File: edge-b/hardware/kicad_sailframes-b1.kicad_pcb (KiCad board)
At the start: 2 copper layers, 79.3 x 73.9 mm, 72 parts, among them J2 JST_PH_BAT, J3 U.FL, J5 MICROSD, J8 BNO085_SOCKET, J9 HOSYOND_3.5_TFT, U1 LC29HEAMD, U2 TP4056, U3 MT3608, U4 ESP32_DEVKIT_V1

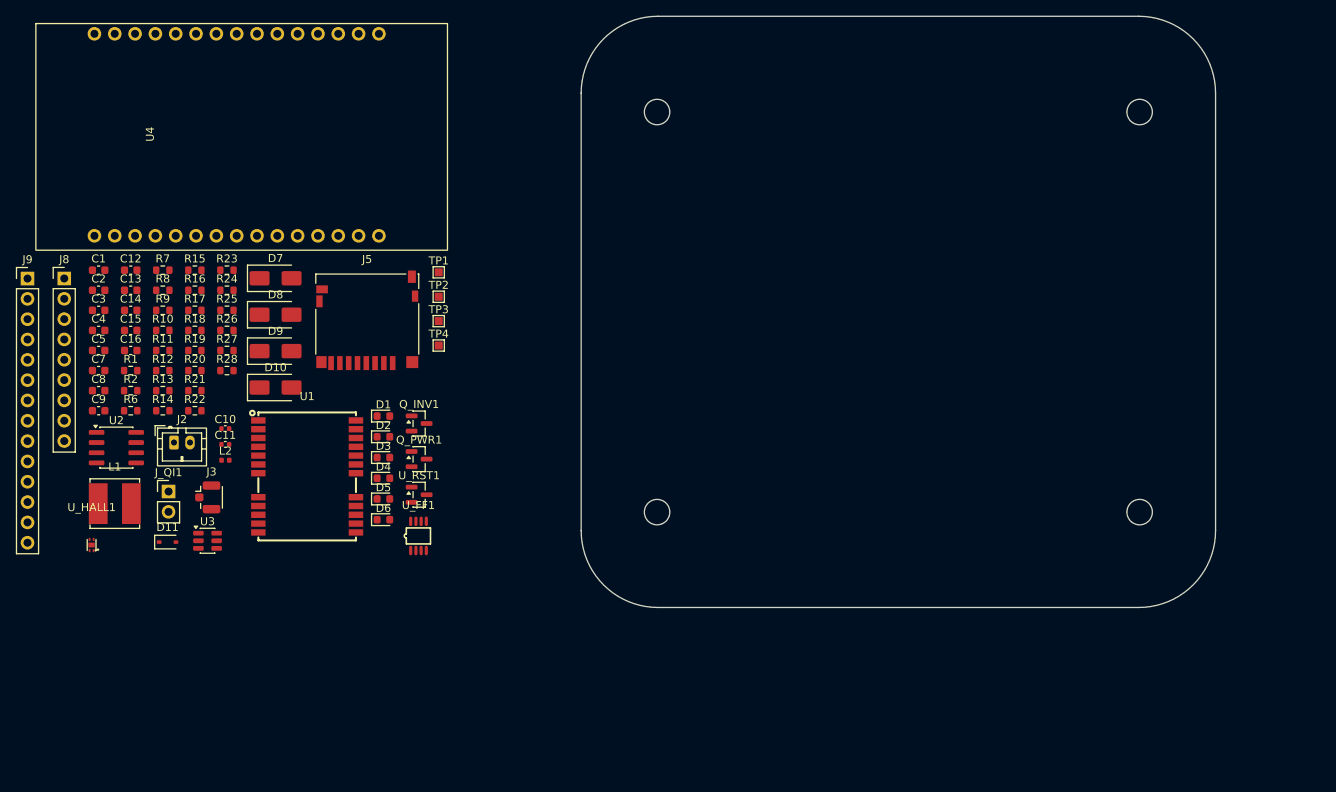
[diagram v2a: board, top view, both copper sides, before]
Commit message: B1 PCB: footprints placed, DRC clean (0 errors)
Update PCB from Schematic synced all 50 components + 6 expansion
connectors (J10-J15) onto the v0.12 outline. Initial placement done
manually in KiCad:

- ESP32 (U4) on B.Cu — wait, on F.Cu (B.Cu reserved for battery contact)
- All components on F.Cu (no components on B.Cu, battery sits underneath)
- L1 boost inductor positioned away from U_HALL1 (magnetic isolation)
- GNSS block (U1, L2, C10, C11, J3) at top-left, RF-clean area
- Power chain (TP4056, MT3608, hall latch) clustered bottom-right
- TFT connector (J9) along bottom edge for cover-side mounting
- microSD (J5) accessible from edge

Board Setup adjustments:
- Default netclass clearance: 0.3 → 0.2 mm (small-pitch IC packages
  like U_HALL1 X2SON-4 and U_FF1 SM8 don't meet 0.3 mm)
- Minimum hole diameter: 0.3 → 0.2 mm (TP4056 SOIC-8-1EP thermal vias)

DRC: 0 errors, 29 cosmetic warnings (silk_overlap + silk_over_copper),
182 unconnected (expected, no routing yet).

Co-Authored-By: Claude Opus 4.7 (1M context) <noreply@anthropic.com>
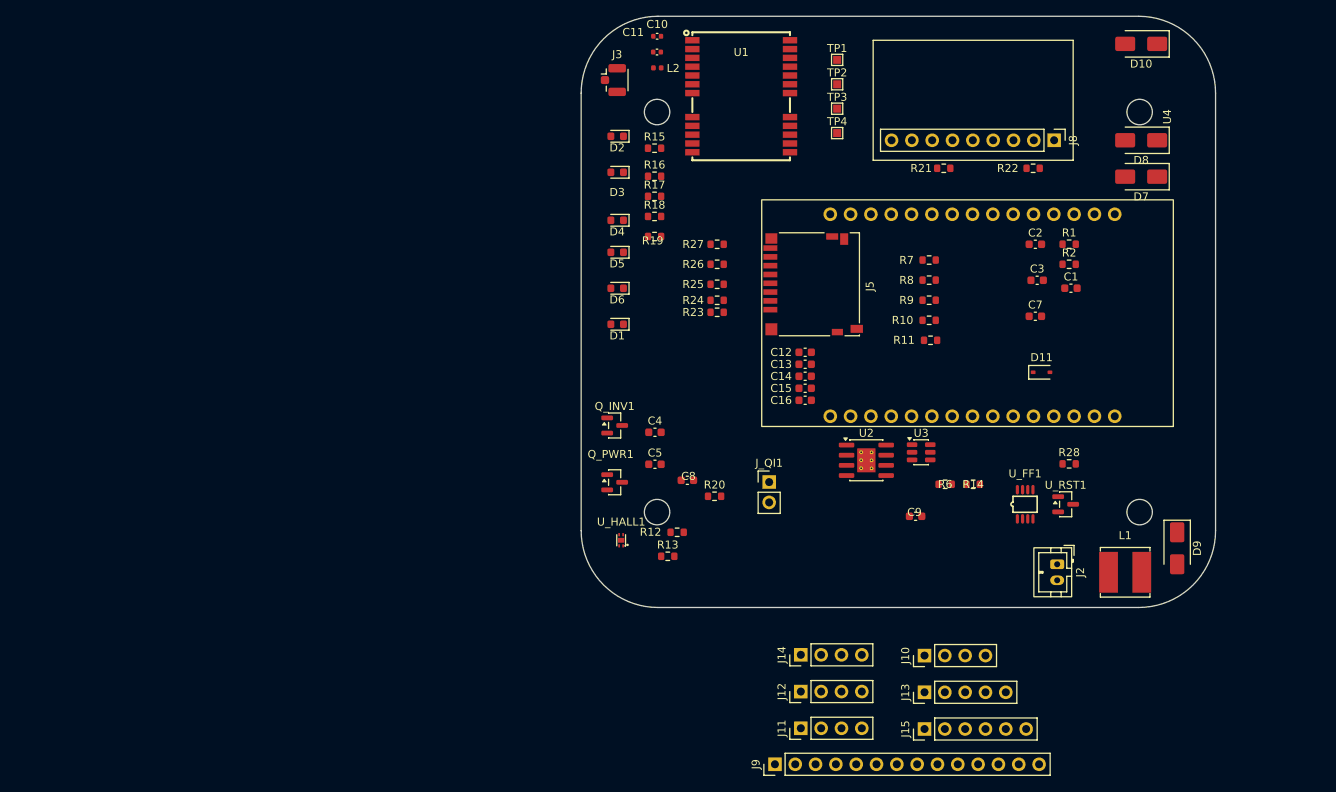
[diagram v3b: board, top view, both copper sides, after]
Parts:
- added J10: I2C_EXP1, Connector_PinHeader_2.54mm:PinHeader_1x04_P2.54mm_Vertical, F.Cu at (142.9, 144.9)
- added J11: I2C_EXP2, Connector_PinHeader_2.54mm:PinHeader_1x04_P2.54mm_Vertical, F.Cu at (127.5, 154.0)
- added J12: I2C_EXP3, Connector_PinHeader_2.54mm:PinHeader_1x04_P2.54mm_Vertical, F.Cu at (127.5, 149.4)
- added J13: GPIO_EXP, Connector_PinHeader_2.54mm:PinHeader_1x05_P2.54mm_Vertical, F.Cu at (142.9, 149.5)
- added J14: UART_DBG, Connector_PinHeader_2.54mm:PinHeader_1x04_P2.54mm_Vertical, F.Cu at (127.5, 144.8)
- added J15: J_AUX, Connector_PinHeader_2.54mm:PinHeader_1x06_P2.54mm_Vertical, F.Cu at (142.9, 154.1)
- U2: footprint Package_SO:SOIC-8_3.9x4.9mm_P1.27mm -> Package_SO:SOIC-8-1EP_3.9x4.9mm_P1.27mm_EP2.29x3mm_ThermalVias
- moved U4 127.6 mm to (166.7, 89.7), turned to 180 degrees
- moved L1 126.6 mm to (168.0, 134.5)
- moved J8 124.9 mm to (159.1, 80.5), turned to -90 degrees
- moved C1 121.6 mm to (161.2, 99.0)
- moved R1 118.4 mm to (161.0, 93.5)
- moved R2 118.4 mm to (161.0, 96.0)
- moved C3 117.4 mm to (157.0, 98.0)
- moved C7 117.3 mm to (156.8, 102.5)
- moved C2 117.2 mm to (156.8, 93.5)
- moved D10 116.4 mm to (170.0, 68.5), turned to 180 degrees
- moved D9 115.4 mm to (174.5, 131.5), turned to -90 degrees
- moved J2 111.4 mm to (159.5, 133.5), turned to -90 degrees
- moved J9 111.4 mm to (124.2, 158.5), turned to 90 degrees
- moved D11 111.3 mm to (157.6, 109.5)
- moved D8 110.4 mm to (170.0, 80.5), turned to 180 degrees
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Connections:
- J2 pad 1: /VBAT -> /GND
- J2 pad 2: /GND -> /VBAT
- U4 pad 12: unconnected-(U4-D12-Pad12) -> /GPIO12
- U4 pad 18: unconnected-(U4-D15-Pad18) -> /GPIO15
- U4 pad 2: unconnected-(U4-VP-Pad2) -> /AUX_INT
- U4 pad 27: unconnected-(U4-RX0-Pad27) -> /RX0
- U4 pad 28: unconnected-(U4-TX0-Pad28) -> /TX0

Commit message: B1 schematic + project specs: add Hosyond TFT footprint, archive specs
B1 KiCad (kicad_sailframes-b1.kicad_sch + .kicad_pcb):
  * Add J9 = HOSYOND_3.5_TFT connector (1x10 2.54mm pin header,
    vertical) for the 3.5" 320x480 ST7796U IPS TFT module also used
    on the E-series enclosures
  * PCB layout + routing updates around the new connector

Project specs at repo root (now tracked):
  * B1_JAUX_HEADER_SPEC.md     — J_AUX expansion header spec
  * SF_FIRMWARE_V2_SPEC.md     — the v2.0.0 firmware roadmap that
    drove the .01 -> .09 Stage 1 work this session
  * SF_SHOPPING_LIST.md        — fleet hardware planning doc

Co-Authored-By: Claude Opus 4.7 (1M context) <noreply@anthropic.com>
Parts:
- J2: footprint Connector_JST:JST_PH_B2B-PH-K_1x02_P2.00mm_Vertical -> Connector_JST:JST_PH_S2B-PH-K_1x02_P2.00mm_Horizontal
- J9: footprint Connector_PinHeader_2.54mm:PinHeader_1x14_P2.54mm_Vertical -> Connector_PinHeader_2.54mm:PinHeader_1x10_P2.54mm_Vertical
- moved C9 36.0 mm to (106.8, 136.0)
- moved U3 35.2 mm to (175.0, 133.0)
- moved J10 24.6 mm to (139.9, 120.5)
- moved J11 24.6 mm to (124.4, 129.6)
- moved J12 24.6 mm to (124.4, 125.0)
- moved J13 24.6 mm to (139.9, 125.1)
- moved J14 24.6 mm to (124.4, 120.4)
- moved J15 24.6 mm to (139.9, 129.7)
- moved J9 23.5 mm to (123.0, 135.0)
- moved U2 21.2 mm to (116.7, 111.0)
- moved U_FF1 16.1 mm to (171.0, 121.5)
- moved R28 15.5 mm to (176.5, 120.0)
- moved U_RST1 15.5 mm to (176.1, 126.0)
- moved D9 14.5 mm to (165.0, 120.5)
- moved R14 13.2 mm to (144.7, 111.0)
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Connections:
- J9 pad 10: /TFT_DC -> /V5_SW
- J9 pad 3: unconnected-(J9-CTP_SDA-Pad3) -> /TFT_BL
- J9 pad 4: unconnected-(J9-CTP_RST-Pad4) -> /VSPI_SCK
- J9 pad 5: unconnected-(J9-CTP_SCL-Pad5) -> /VSPI_MOSI
- J9 pad 6: unconnected-(J9-SDO_MISO-Pad6) -> /TFT_DC
- J9 pad 7: /TFT_BL -> /TFT_RST
- J9 pad 8: /VSPI_SCK -> /TFT_CS
- J9 pad 9: /VSPI_MOSI -> /GND
